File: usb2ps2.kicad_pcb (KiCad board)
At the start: 2 copper layers, 54.4 x 33.1 mm, 55 parts, among them CN1 Conn_01x03_Pin, CN2 UART, CN3 PS/2 Pins, SW1 Flash Button, U1 NCP1117-3.3_SOT223, Y1 ABM8-272-T3

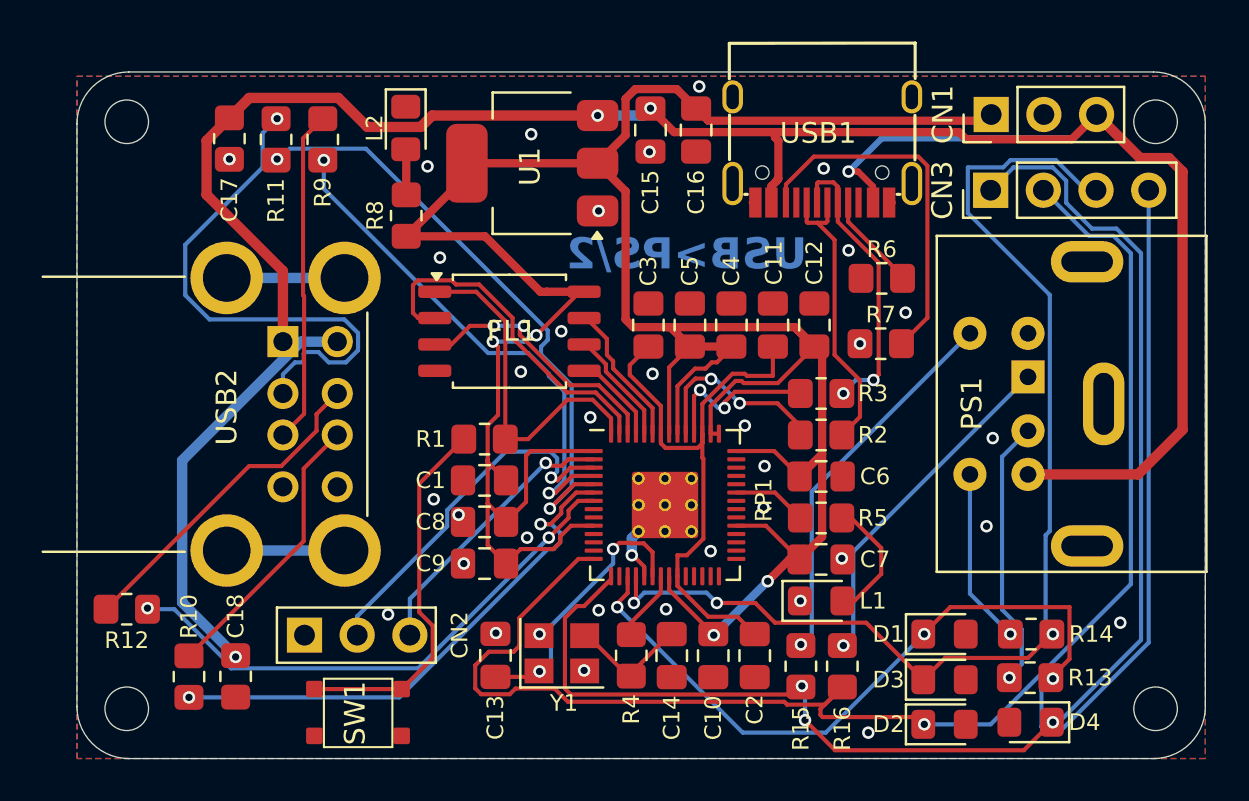
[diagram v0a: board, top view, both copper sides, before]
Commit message: HW Rev 1.2 minor fixes
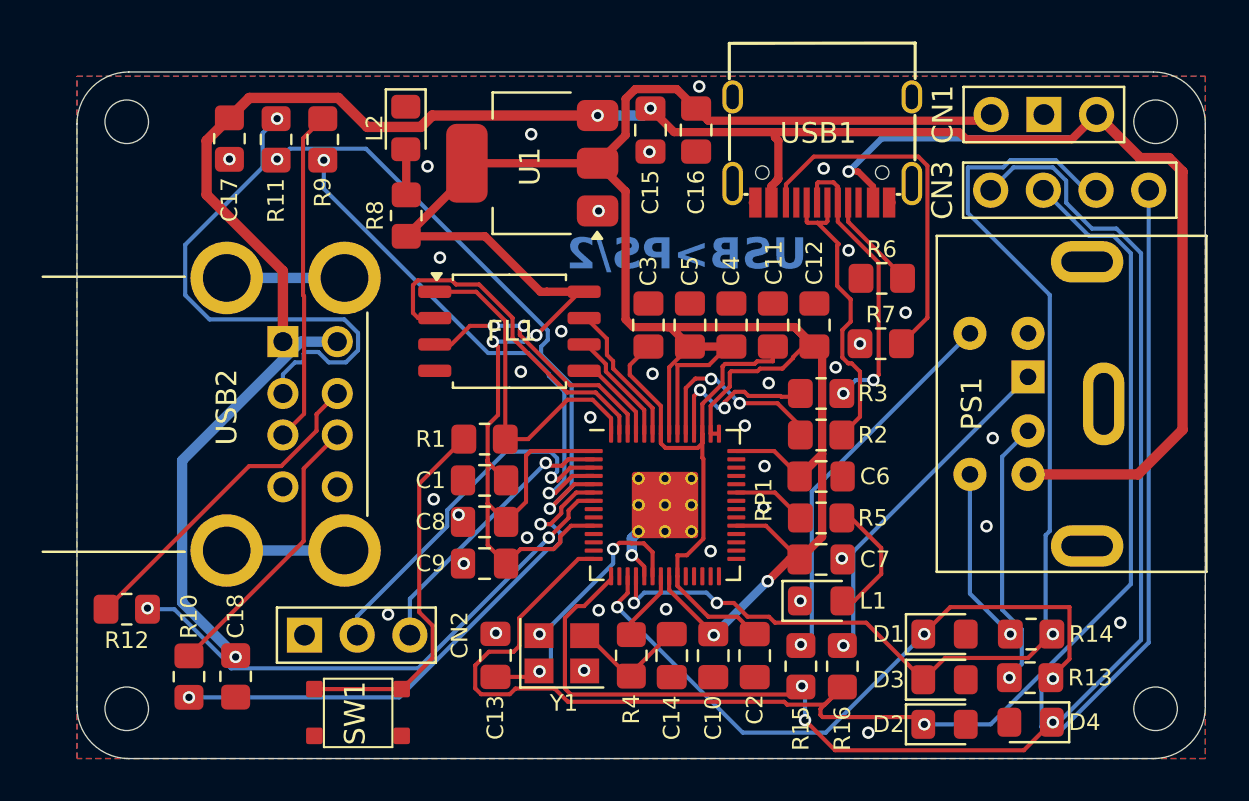
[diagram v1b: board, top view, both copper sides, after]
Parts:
- CN1: footprint Connector_PinHeader_2.54mm:PinHeader_1x03_P2.54mm_Vertical -> LIBS:Medved_PinHeader_1x03
- CN3: footprint Connector_PinHeader_2.54mm:PinHeader_1x04_P2.54mm_Vertical -> LIBS:Medved_PinHeader_1x04
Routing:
- net +3V3: track 143.0 -> 143.9 mm
- net GND: vias 36 -> 38
